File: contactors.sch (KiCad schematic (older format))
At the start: 0 parts

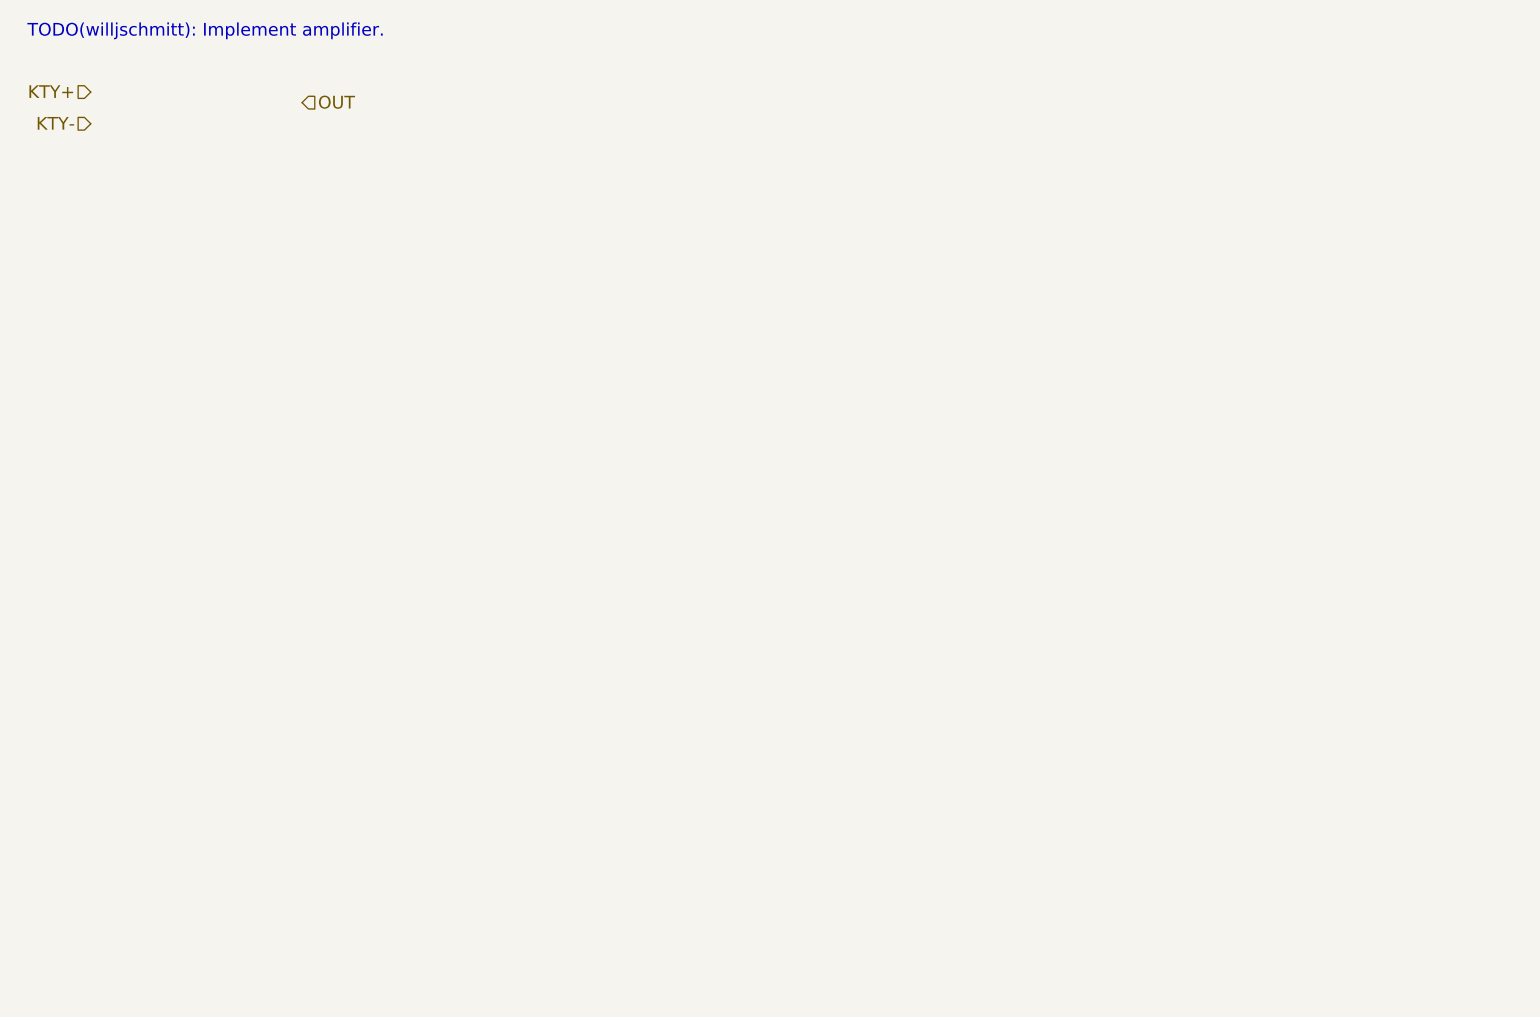
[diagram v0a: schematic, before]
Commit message: Adding contactor placeholders.
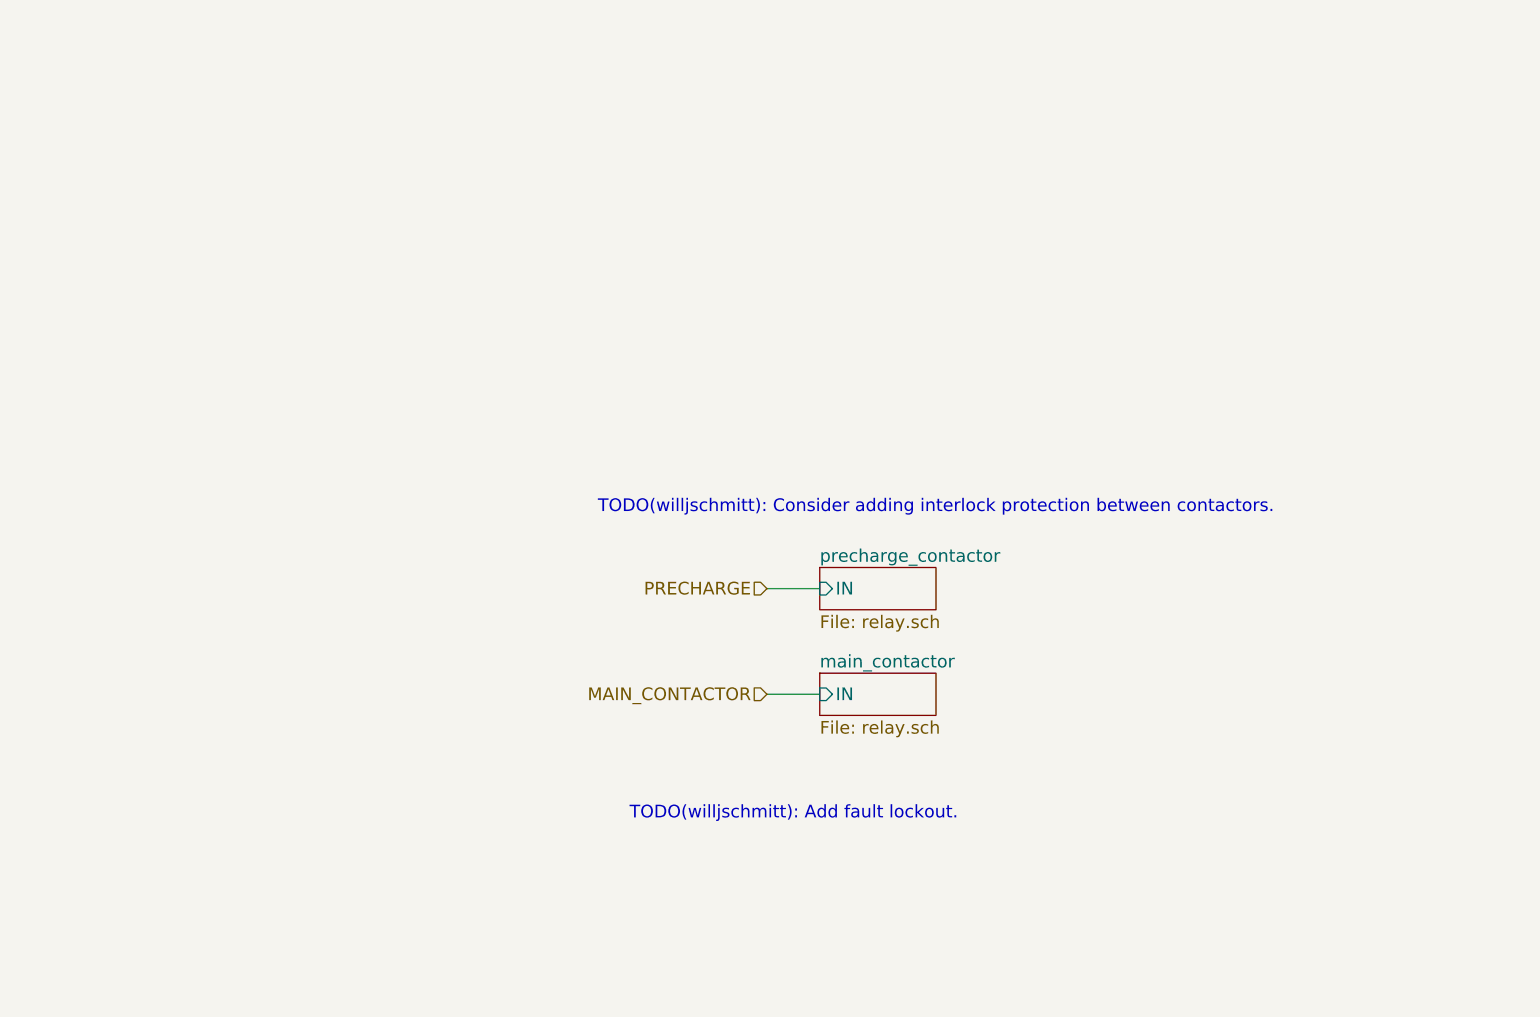
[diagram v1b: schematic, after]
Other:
- note added: "TODO(willjschmitt): Add fault lockout."
- note added: "TODO(willjschmitt): Consider adding interlock protection between contactors."
- note removed: "TODO(willjschmitt): Implement amplifier."
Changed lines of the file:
@@
 $Descr A4 11693 8268
 encoding utf-8
-Sheet 13 18
+Sheet 16 18
 Title ""
 Date ""
@@
 Comment4 ""
 $EndDescr
-Text HLabel 2150 1300 0    60   Input ~ 0
-KTY+
-Text HLabel 2150 1450 0    60   Input ~ 0
-KTY-
-Text HLabel 3150 1350 2    60   Input ~ 0
-OUT
-Text Notes 1850 1050 0    60   ~ 0
-TODO(willjschmitt): Implement amplifier.
+$Sheet
+S 5600 3550 550  200
+U 5AFF30F9
+F0 "precharge_contactor" 60
+F1 "relay.sch" 60
+F2 "IN" I L 5600 3650 60
+$EndSheet
+Text HLabel 5350 3650 0    60   Input ~ 0
+PRECHARGE
+Text HLabel 5350 4150 0    60   Input ~ 0
+MAIN_CONTACTOR
+Wire Wire Line
+	5600 3650 5350 3650
+$Sheet
+S 5600 4050 550  200
+U 5AFF3733
+F0 "main_contactor" 60
+F1 "relay.sch" 60
+F2 "IN" I L 5600 4150 60
+$EndSheet
+Wire Wire Line
+	5600 4150 5350 4150
+Text Notes 4550 3300 0    60   ~ 0
+TODO(willjschmitt): Consider adding interlock protection between contactors.
+Text Notes 4700 4750 0    60   ~ 0
+TODO(willjschmitt): Add fault lockout.
 $EndSCHEMATC

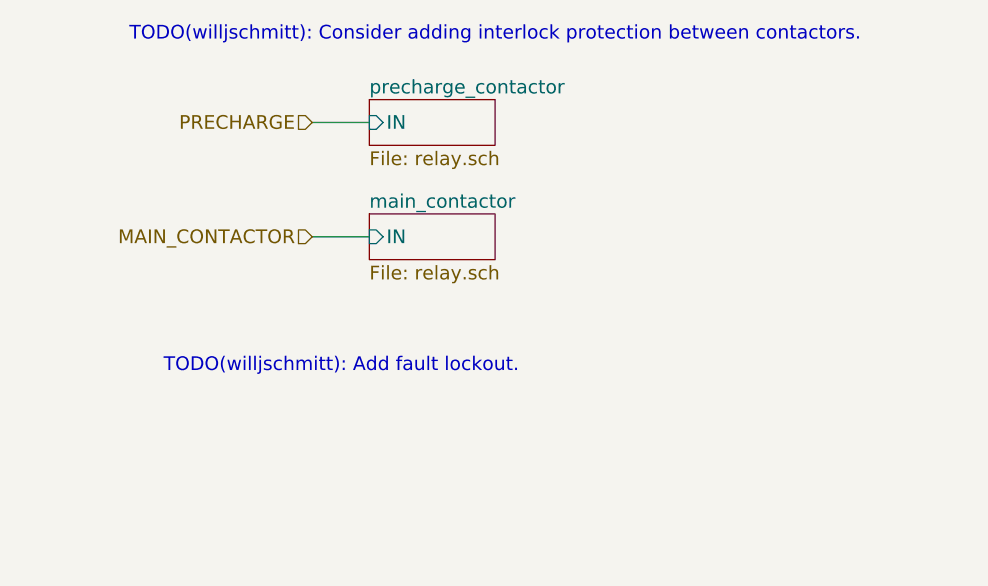
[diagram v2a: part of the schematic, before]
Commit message: Add fault lockout to relays.
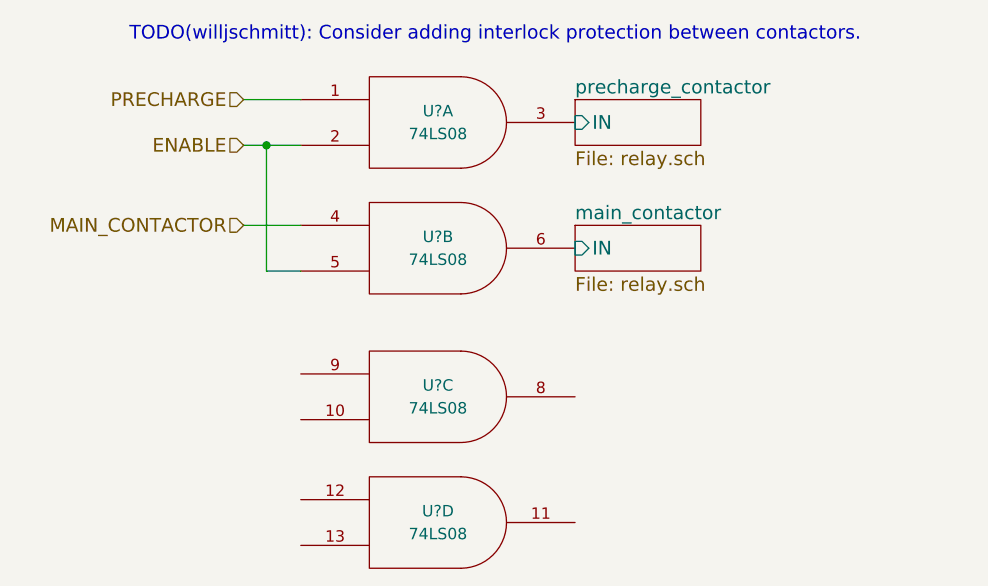
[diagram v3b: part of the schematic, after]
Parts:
- added U? (x4): 74LS08, symbol 74LS08
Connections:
- net MAIN_CONTACTOR: now also U?.4
- net PRECHARGE: now also U?.1
- new net ENABLE: U?.2, U?.5
- new net GND: U?.7 (GND), U?.7 (GND), U?.7 (GND), U?.7 (GND)
- new net VCC: U?.14 (VCC), U?.14 (VCC), U?.14 (VCC), U?.14 (VCC)
- new net main_contactor/IN: U?.6
- new net precharge_contactor/IN: U?.3
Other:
- note removed: "TODO(willjschmitt): Add fault lockout."
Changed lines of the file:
@@
 $EndDescr
 $Sheet
-S 5600 3550 550  200
+S 6500 3550 550  200
 U 5AFF30F9
 F0 "precharge_contactor" 60
 F1 "relay.sch" 60
-F2 "IN" I L 5600 3650 60
+F2 "IN" I L 6500 3650 60
 $EndSheet
-Text HLabel 5350 3650 0    60   Input ~ 0
+Text HLabel 5050 3550 0    60   Input ~ 0
 PRECHARGE
-Text HLabel 5350 4150 0    60   Input ~ 0
+Text HLabel 5050 4100 0    60   Input ~ 0
 MAIN_CONTACTOR
 Wire Wire Line
-	5600 3650 5350 3650
+	5300 3550 5050 3550
 $Sheet
-S 5600 4050 550  200
+S 6500 4100 550  200
 U 5AFF3733
 F0 "main_contactor" 60
 F1 "relay.sch" 60
-F2 "IN" I L 5600 4150 60
+F2 "IN" I L 6500 4200 60
 $EndSheet
-Wire Wire Line
-	5600 4150 5350 4150
 Text Notes 4550 3300 0    60   ~ 0
 TODO(willjschmitt): Consider adding interlock protection between contactors.
-Text Notes 4700 4750 0    60   ~ 0
-TODO(willjschmitt): Add fault lockout.
+$Comp
+L 74LS08 U?
+U 1 1 5AEF0674
+P 5900 3650
+F 0 "U?" H 5900 3700 50  0000 C CNN
+F 1 "74LS08" H 5900 3600 50  0000 C CNN
+F 2 "" H 5900 3650 50  0001 C CNN
+F 3 "" H 5900 3650 50  0001 C CNN
+	1    5900 3650
+	1    0    0    -1
+$EndComp
+$Comp
+L 74LS08 U?
+U 2 1 5AEF06F2
+P 5900 4200
+F 0 "U?" H 5900 4250 50  0000 C CNN
+F 1 "74LS08" H 5900 4150 50  0000 C CNN
+F 2 "" H 5900 4200 50  0001 C CNN
+F 3 "" H 5900 4200 50  0001 C CNN
+	2    5900 4200
+	1    0    0    -1
+$EndComp
+$Comp
+L 74LS08 U?
+U 3 1 5AEF0769
+P 5900 4850
+F 0 "U?" H 5900 4900 50  0000 C CNN
+F 1 "74LS08" H 5900 4800 50  0000 C CNN
+F 2 "" H 5900 4850 50  0001 C CNN
+F 3 "" H 5900 4850 50  0001 C CNN
+	3    5900 4850
+	1    0    0    -1
+$EndComp
+$Comp
+L 74LS08 U?
+U 4 1 5AEF07D8
+P 5900 5400
+F 0 "U?" H 5900 5450 50  0000 C CNN
+F 1 "74LS08" H 5900 5350 50  0000 C CNN
+F 2 "" H 5900 5400 50  0001 C CNN
+F 3 "" H 5900 5400 50  0001 C CNN
+	4    5900 5400
+	1    0    0    -1
+$EndComp
+Text HLabel 5050 3750 0    60   Input ~ 0
+ENABLE
+Wire Wire Line
+	5050 3750 5300 3750
+Wire Wire Line
+	5050 4100 5300 4100
+Wire Wire Line
+	5150 3750 5150 4300
+Wire Wire Line
+	5150 4300 5300 4300
+Connection ~ 5150 3750
 $EndSCHEMATC

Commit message: Annotate and add negative IOC faults.
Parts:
- gave numbers to parts that had none: 1
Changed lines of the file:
@@
 TODO(willjschmitt): Consider adding interlock protection between contactors.
 $Comp
-L 74LS08 U?
+L 74LS08 U13
 U 1 1 5AEF0674
 P 5900 3650
-F 0 "U?" H 5900 3700 50  0000 C CNN
+F 0 "U13" H 5900 3700 50  0000 C CNN
 F 1 "74LS08" H 5900 3600 50  0000 C CNN
 F 2 "" H 5900 3650 50  0001 C CNN
@@
 $EndComp
 $Comp
-L 74LS08 U?
+L 74LS08 U13
 U 2 1 5AEF06F2
 P 5900 4200
-F 0 "U?" H 5900 4250 50  0000 C CNN
+F 0 "U13" H 5900 4250 50  0000 C CNN
 F 1 "74LS08" H 5900 4150 50  0000 C CNN
 F 2 "" H 5900 4200 50  0001 C CNN
@@
 $EndComp
 $Comp
-L 74LS08 U?
+L 74LS08 U13
 U 3 1 5AEF0769
 P 5900 4850
-F 0 "U?" H 5900 4900 50  0000 C CNN
+F 0 "U13" H 5900 4900 50  0000 C CNN
 F 1 "74LS08" H 5900 4800 50  0000 C CNN
 F 2 "" H 5900 4850 50  0001 C CNN
@@
 $EndComp
 $Comp
-L 74LS08 U?
+L 74LS08 U13
 U 4 1 5AEF07D8
 P 5900 5400
-F 0 "U?" H 5900 5450 50  0000 C CNN
+F 0 "U13" H 5900 5450 50  0000 C CNN
 F 1 "74LS08" H 5900 5350 50  0000 C CNN
 F 2 "" H 5900 5400 50  0001 C CNN
